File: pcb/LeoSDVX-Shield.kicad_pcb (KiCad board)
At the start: 2 copper layers, 68.6 x 53.3 mm, 11 parts, among them J1 JST-XH, J10 Conn_01x02, J2 JST-XH, J3 JST-XH, J4 JST-XH, J5 JST-XH, J6 JST-XH, J7 JST-XH, J8 JST-XH, J9 JST-XH

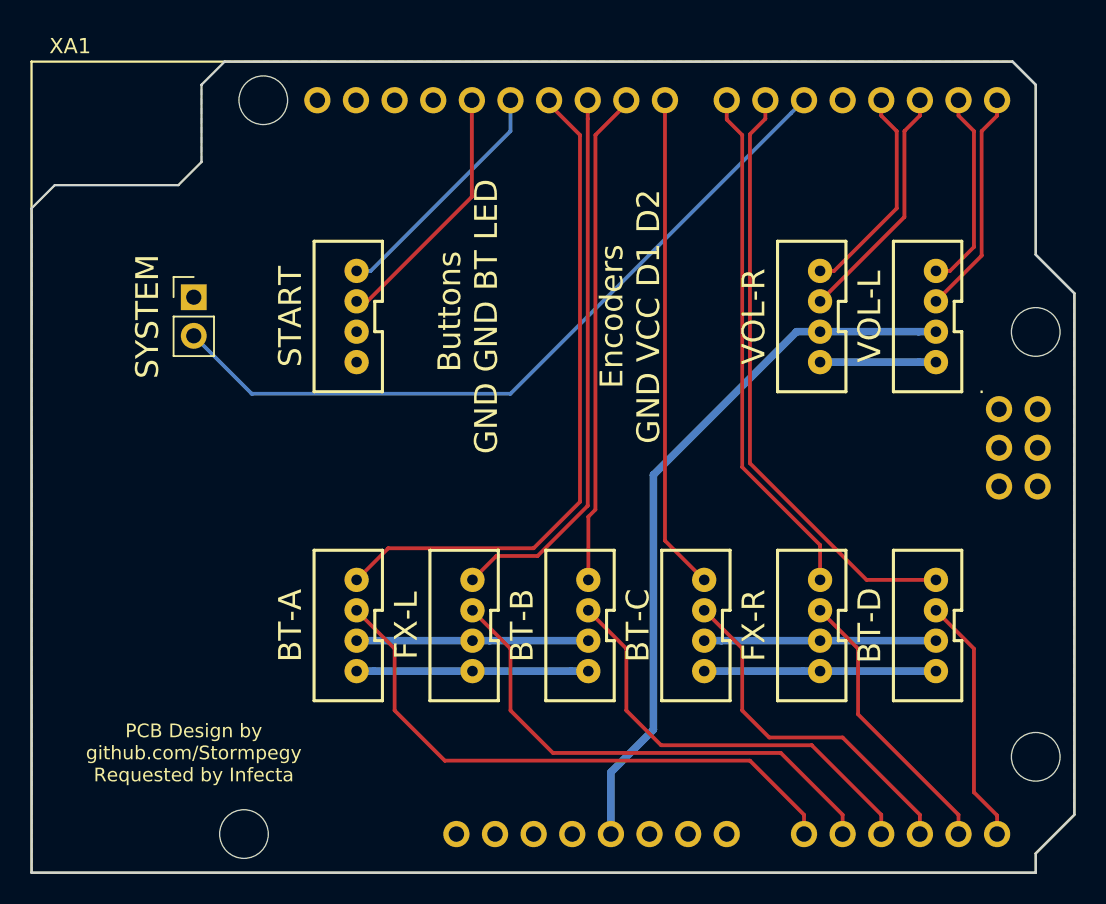
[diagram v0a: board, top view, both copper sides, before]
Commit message: Revision 2
REV 2 released

- Replaced JST-XH connector footprints with generic 2.54mm header footprints, original footprints were well out of spec and didn't fit 2.54mm headers/plugs; thank you SirusDoma (C&S discord) for bringing this to my attention.

- System pin rotated to have GND on the same side as all other connections (I have also forgotten why the system pin exists but I'm leaving it there /shrug)

- Removed white border on leonardo shield footprint, library updated and included

Hopefully the last update this will need
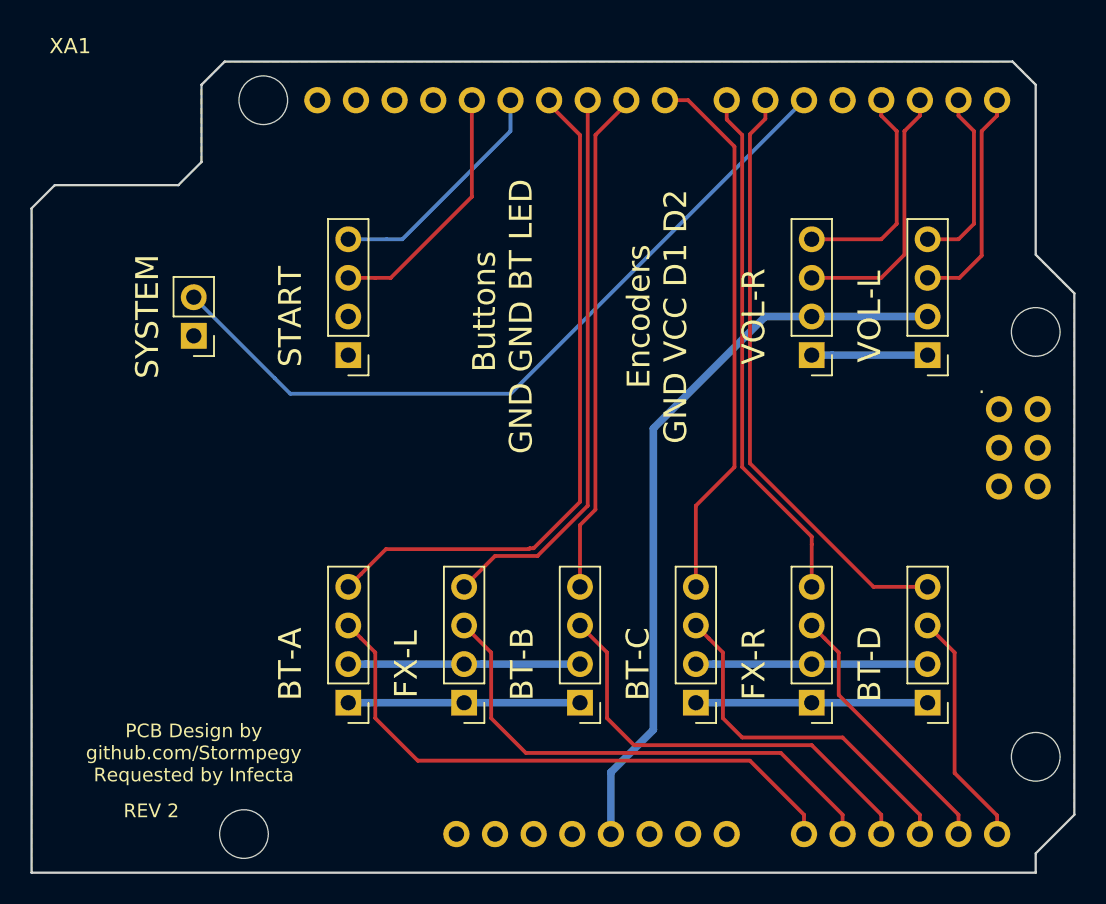
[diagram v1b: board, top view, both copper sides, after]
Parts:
- J1, J2, J3, J4, J5, J6, J7, J8, J9: value JST-XH -> CONN_04; footprint Connectors:JST-4-PTH-VERT -> Pin_Headers:Pin_Header_Straight_1x04_Pitch2.54mm
- XA1: footprint Arduino:Arduino_Leonardo_Shield -> Arduino:Arduino_Leonardo_Shield_noborder
- moved J4 5.08 mm to (167.6, 91.4), turned to 180 degrees
- moved J5 5.08 mm to (175.3, 91.4), turned to 180 degrees
- moved J6 5.08 mm to (182.9, 91.4), turned to 180 degrees
- moved J7 5.08 mm to (190.5, 91.4), turned to 180 degrees
- moved J8 5.08 mm to (198.1, 91.4), turned to 180 degrees
- moved J9 5.08 mm to (205.7, 91.4), turned to 180 degrees
- moved J10 2.54 mm to (157.5, 67.3), turned to 180 degrees
- moved J1 2.54 mm to (205.7, 68.6), turned to 180 degrees
- moved J2 2.54 mm to (198.1, 68.6), turned to 180 degrees
- moved J3 2.54 mm to (167.6, 68.6), turned to 180 degrees
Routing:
- net /B5LED: track 32.6 -> 35.8 mm
- net /VCC: track 47.3 -> 48.9 mm
- net /E2D-: track 15.9 -> 17.3 mm
- net /E1D+: track 13.2 -> 12.0 mm
- net Net-(J10-Pad2): track 49.7 -> 50.8 mm
- net /B7: track 16.4 -> 15.6 mm
- net /B6: track 18.5 -> 17.7 mm
- net /B2LED: track 44.1 -> 44.8 mm
- net /B3LED: track 36.3 -> 37.0 mm
- net /B4LED: track 32.6 -> 33.3 mm
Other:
- board text added: "REV 2"
